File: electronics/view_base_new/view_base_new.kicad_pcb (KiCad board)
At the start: 2 copper layers, 81.2 x 81.2 mm, 107 parts, among them J1 BLDC, J2 USB_C_Receptacle_USB2.0, J3 LCD, J4 A, J5 B, Q1 MMBT4403, Q2 UMH3N, U1 MT6701-CT, U2 T-Micro32_Plus, U3 CH340C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

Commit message: improve routing
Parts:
- removed C11: 0.1uF, Capacitor_SMD:C_0603_1608Metric
- removed J4: A, SolderPads:SolderPads_2mm_3_STRAIN
- removed J5: B, SolderPads:SolderPads_2mm_3_STRAIN
- removed Q2: UMH3N, Package_TO_SOT_SMD:SOT-363_SC-70-6
- removed R1, R2: 5.1k, Resistor_SMD:R_0603_1608Metric
- removed TP13: EN, Modified:TestPoint_Pad_D2.0mm_ValueSilk
- removed TP14: BOOT, Modified:TestPoint_Pad_D2.0mm_ValueSilk
- removed U3: CH340C, Package_SO:SOIC-16_3.9x9.9mm_P1.27mm
- removed U6: AP2114HA-3.3, Modified:SOT-223-3_TabPin2_InGndOut
- C26: moved to B.Cu
- J2: value USB_C_Receptacle_USB2.0 -> Conn_01x06_Socket; footprint GCT_USB:USB4510_NoPaste -> Connector_PinHeader_2.54mm:PinHeader_1x06_P2.54mm_Vertical
- moved J2 6.66 mm to (93.7, 138.6), turned to 90 degrees
- moved R17 4.22 mm to (83.6, 133.2), turned to 90 degrees
- moved TP15 4.00 mm to (87.0, 133.0)
- moved R7 3.20 mm to (125.8, 134.5)
- moved R16 2.95 mm to (71.2, 109.2), turned to 90 degrees
- moved R8 2.90 mm to (127.6, 134.5)
- moved R9 2.60 mm to (129.4, 134.5)
- moved C10 2.48 mm to (119.6, 135.6), turned to 0 degrees
- moved R10 2.30 mm to (131.2, 134.5)
- moved R14 2.22 mm to (65.8, 109.2), turned to -90 degrees
- moved R11 2.00 mm to (133.0, 134.5)
- moved TP16 1.80 mm to (84.8, 130.0)
- moved R12 1.70 mm to (134.8, 134.5)
- moved C9 1.63 mm to (119.6, 133.2), turned to 0 degrees
- moved C16 1.51 mm to (67.0, 81.2)
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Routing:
- net +3V3: track 340.1 -> 304.6 mm, vias 14 -> 8
- net /USB_D+: track 21.6 -> 0.00 mm, vias 2 -> 0
- net /USB_D-: track 21.1 -> 0.00 mm
- net +5V: track 256.1 -> 237.2 mm, vias 8 -> 4
- net /DTR: track 17.4 -> 0.00 mm, vias 2 -> 0
- net /USB_SERIAL_TXO: track 22.8 -> 39.2 mm, vias 2 -> 1
- net /RTS: track 16.4 -> 0.00 mm
- net /ESP32_EN: track 15.4 -> 30.9 mm, vias 1 -> 0
- net /USB_SERIAL_RXI: track 23.0 -> 35.9 mm, vias 2 -> 1
- net /ESP32_BOOT: track 34.9 -> 47.6 mm, vias 3 -> 1
- net /STRAIN_E+: track 119.0 -> 106.4 mm, vias 4 -> 2
- net GND: track 69.1 -> 59.2 mm, vias 47 -> 52
- net /STRAIN_S+: track 75.0 -> 66.0 mm, vias 2 -> 1
- net Net-(J1-Pin_3): track 18.4 -> 11.3 mm
- net /SCL: track 104.2 -> 97.9 mm, vias 4 -> 2
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- removed copper zone on F.Cu, net +5V
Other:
- outline, holes or cut-outs redrawn

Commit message: tuning routing, save work
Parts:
- C25, C27, C28, C29: footprint Capacitor_SMD:C_0603_1608Metric -> Capacitor_SMD:C_0603_1608Metric_Pad1.08x0.95mm_HandSolder
- C26: footprint Capacitor_SMD:C_0805_2012Metric -> Capacitor_SMD:C_0805_2012Metric_Pad1.18x1.45mm_HandSolder
- moved C15 1.42 mm to (124.6, 125.8)
- moved L1 1.39 mm to (75.8, 76.7), turned to -90 degrees
- moved C19 0.50 mm to (77.6, 77.0)
- moved C13 0.40 mm to (121.8, 122.6)
- moved C18 0.30 mm to (79.6, 76.8)
- moved C25 0.22 mm to (79.4, 134.9)
- moved C28 0.21 mm to (79.4, 131.3)
- moved C14 0.20 mm to (123.8, 122.6)
- moved R17 0.20 mm to (83.8, 133.2)
- moved C24 0.20 mm to (81.6, 135.0)
- moved C27 0.06 mm to (99.9, 64.5)
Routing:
- net +5V: track 237.2 -> 228.2 mm, vias 4 -> 5
- net GND: track 59.2 -> 64.1 mm, vias 52 -> 64
- net /STRAIN_S-: track 42.7 -> 38.1 mm
- net /STRAIN_E+: track 106.4 -> 109.7 mm
- net /TMC_UL: track 68.6 -> 70.4 mm
- net /TMC_WL: track 72.2 -> 74.0 mm
- net /TMC_VL: track 77.2 -> 79.0 mm
- net Net-(U5-VCP): track 2.69 -> 3.96 mm
- net Net-(Q1-C): track 10.5 -> 11.6 mm
- net /TMC_VH: track 64.3 -> 63.3 mm
- net /LED_DATA_5V: track 18.3 -> 19.2 mm
- net /TMC_WH: track 67.3 -> 66.4 mm, vias 4 -> 2
- net +3V3: track 304.6 -> 305.2 mm
- net /TMC_UH: track 66.8 -> 67.3 mm
- net GNDA: track 70.4 -> 70.6 mm, vias 38 -> 43

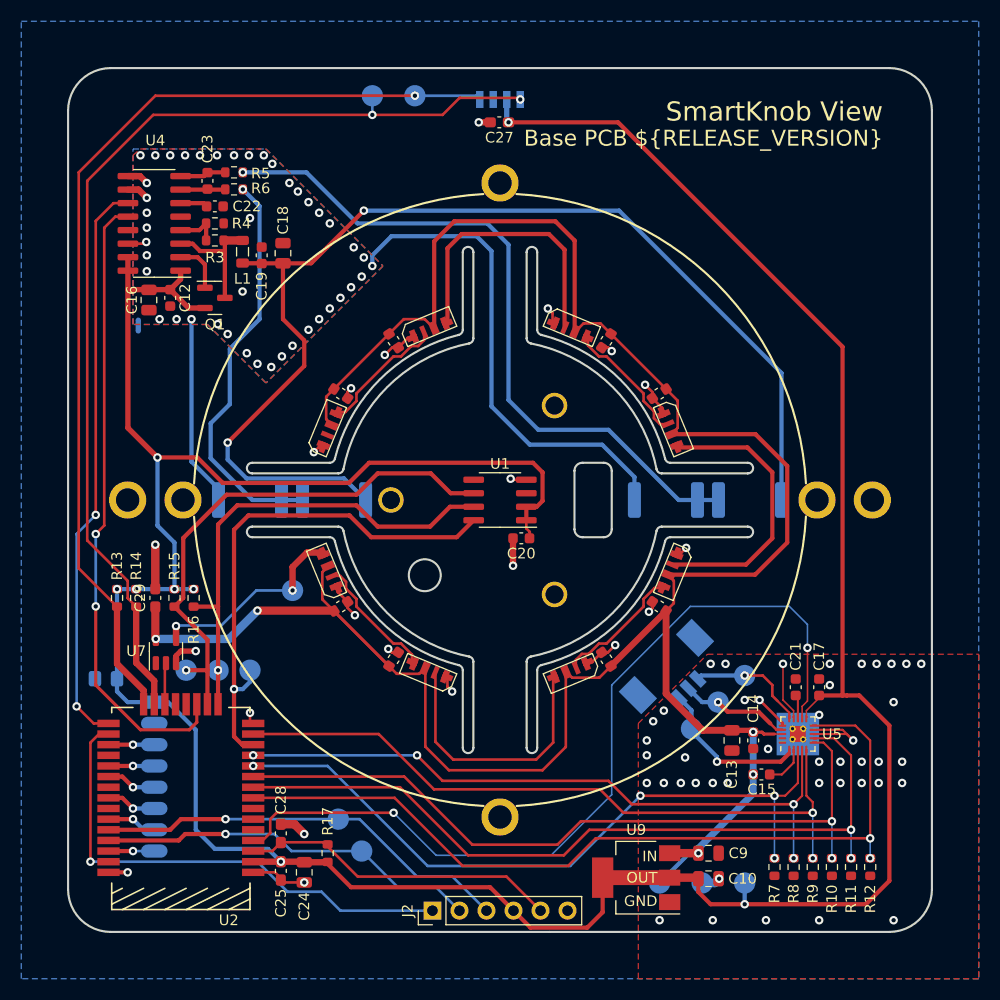
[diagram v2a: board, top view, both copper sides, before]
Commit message: change to hand soldering pad
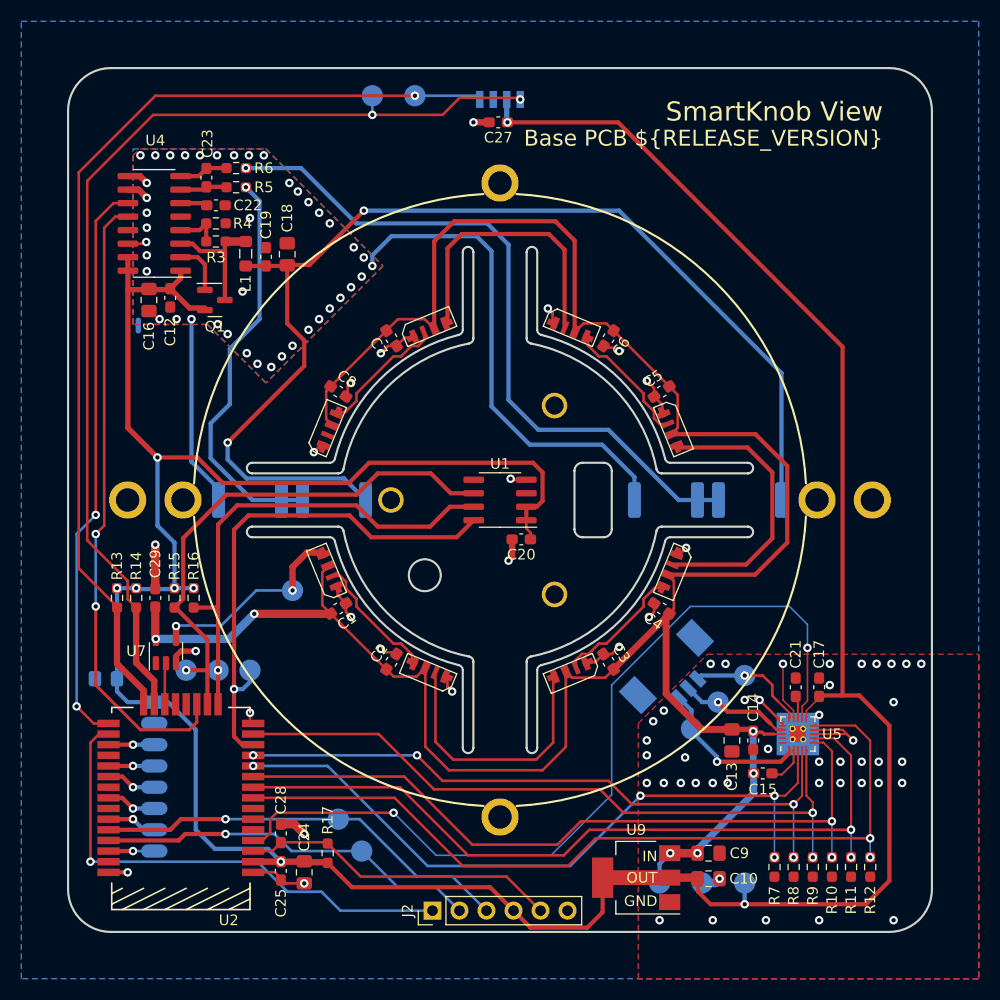
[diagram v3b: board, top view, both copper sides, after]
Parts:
- C1, C12, C14, C15, C17, C19, C2, C20, C21, C22, C23, C3, C4, C5, C6, C7, C8: footprint Capacitor_SMD:C_0603_1608Metric -> Capacitor_SMD:C_0603_1608Metric_Pad1.08x0.95mm_HandSolder
- C10, C13, C16, C18, C24, C9: footprint Capacitor_SMD:C_0805_2012Metric -> Capacitor_SMD:C_0805_2012Metric_Pad1.18x1.45mm_HandSolder
- L1: footprint Inductor_SMD:L_0805_2012Metric -> Inductor_SMD:L_0805_2012Metric_Pad1.05x1.20mm_HandSolder
- R10, R11, R12, R13, R14, R15, R16, R17, R3, R4, R5, R6, R7, R8, R9: footprint Resistor_SMD:R_0603_1608Metric -> Resistor_SMD:R_0603_1608Metric_Pad0.98x0.95mm_HandSolder
- moved R6 0.45 mm to (75.2, 68.8)
- moved C19 0.42 mm to (78.0, 77.1)
- moved C18 0.41 mm to (80.0, 76.9)
- moved L1 0.35 mm to (76.1, 76.8)
- moved C23 0.32 mm to (72.4, 69.7)
- moved C1 0.31 mm to (84.8, 110.2)
- moved C2 0.31 mm to (89.8, 115.2)
- moved C3 0.31 mm to (110.2, 115.2)
- moved C4 0.31 mm to (115.2, 110.2)
- moved C5 0.31 mm to (115.2, 89.8)
- moved C6 0.31 mm to (110.2, 84.8)
- moved C7 0.31 mm to (89.8, 84.8)
- moved C8 0.31 mm to (84.8, 89.8)
- moved R5 0.28 mm to (75.2, 70.6)
- moved Q1 0.20 mm to (73.2, 81.2)
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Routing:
- net +5V: track 228.2 -> 220.3 mm, vias 5 -> 6
- net GND: track 64.1 -> 67.1 mm
- net /STRAIN_E+: track 109.7 -> 107.2 mm
- net Net-(U4-INA-): track 4.21 -> 4.76 mm
- net GNDA: vias 43 -> 42
